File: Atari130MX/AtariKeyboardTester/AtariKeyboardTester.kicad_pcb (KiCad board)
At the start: 2 copper layers, 117 parts, among them J1 Conn_01x24, J2 Conn_02x12_Odd_Even, J3 Conn_01x26

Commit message: WIP keyboard tester
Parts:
- removed D12, D14, D15, D21, D23, D24, D28, D36, D43, D5, D50, D56, D57, D61, D64, D8, D_COL_1, D_COL_10, D_COL_11, D_COL_12, D_COL_13, D_COL_2, D_COL_3, D_COL_4, D_COL_5, D_COL_6, D_COL_7, D_COL_8, D_COL_9, D_ROW_1, D_ROW_10, D_ROW_2, D_ROW_3, D_ROW_4, D_ROW_5, D_ROW_6, D_ROW_7, D_ROW_8, D_ROW_9: LED, LED_THT:LED_D3.0mm
- added D_1_1: LED, LED_THT:LED_D3.0mm, F.Cu at (25.4, 22.9)
- added D_2_1: LED, LED_THT:LED_D3.0mm, F.Cu at (30.5, 22.9)
- added D_3_1: LED, LED_THT:LED_D3.0mm, F.Cu at (35.6, 22.9)
- added D_=_1: LED, LED_THT:LED_D3.0mm, F.Cu at (83.8, 27.9)
- added D_A_10: LED, LED_THT:LED_D3.0mm, F.Cu at (163.4, 93.0)
- added D_A_11: LED, LED_THT:LED_D3.0mm, F.Cu at (132.3, 122.4)
- added D_A_12: LED, LED_THT:LED_D3.0mm, F.Cu at (157.5, 98.5)
- added D_A_13: LED, LED_THT:LED_D3.0mm, F.Cu at (125.2, 129.2)
- added D_A_14: LED, LED_THT:LED_D3.0mm, F.Cu at (151.0, 104.1)
- added D_A_15: LED, LED_THT:LED_D3.0mm, F.Cu at (101.6, 152.5)
- added D_A_16: LED, LED_THT:LED_D3.0mm, F.Cu at (128.6, 116.9)
- added D_A_17: LED, LED_THT:LED_D3.0mm, F.Cu at (135.2, 110.8)
- added D_A_18: LED, LED_THT:LED_D3.0mm, F.Cu at (141.1, 110.2)
- added D_A_19: LED, LED_THT:LED_D3.0mm, F.Cu at (134.5, 116.9)
- added D_A_2: LED, LED_THT:LED_D3.0mm, F.Cu at (116.8, 118.1)
- added D_A_20: LED, LED_THT:LED_D3.0mm, F.Cu at (101.6, 147.0)
- added D_A_21: LED, LED_THT:LED_D3.0mm, F.Cu at (95.7, 155.7)
- added D_A_22: LED, LED_THT:LED_D3.0mm, F.Cu at (112.8, 141.4)
- added D_A_23: LED, LED_THT:LED_D3.0mm, F.Cu at (157.5, 93.0)
- added D_A_24: LED, LED_THT:LED_D3.0mm, F.Cu at (126.4, 123.7)
- added D_A_25: LED, LED_THT:LED_D3.0mm, F.Cu at (151.6, 98.5)
- added D_A_3: LED, LED_THT:LED_D3.0mm, F.Cu at (118.7, 135.9)
- added D_A_4: LED, LED_THT:LED_D3.0mm, F.Cu at (132.3, 128.0)
- added D_A_5: LED, LED_THT:LED_D3.0mm, F.Cu at (107.5, 152.5)
- added D_A_6: LED, LED_THT:LED_D3.0mm, F.Cu at (125.2, 134.8)
- added D_A_7: LED, LED_THT:LED_D3.0mm, F.Cu at (118.7, 141.4)
- added D_A_8: LED, LED_THT:LED_D3.0mm, F.Cu at (141.1, 115.8)
- added D_A_9: LED, LED_THT:LED_D3.0mm, F.Cu at (146.9, 109.7)
- added D_B_10: LED, LED_THT:LED_D3.0mm, F.Cu at (151.6, 93.0)
- added D_B_11: LED, LED_THT:LED_D3.0mm, F.Cu at (120.5, 123.7)
- added D_B_12: LED, LED_THT:LED_D3.0mm, F.Cu at (106.9, 135.9)
- added D_B_13: LED, LED_THT:LED_D3.0mm, F.Cu at (129.2, 111.3)
- added D_B_14: LED, LED_THT:LED_D3.0mm, F.Cu at (139.2, 104.7)
- added D_B_15: LED, LED_THT:LED_D3.0mm, F.Cu at (145.7, 98.5)
- added D_B_16: LED, LED_THT:LED_D3.0mm, F.Cu at (89.8, 150.1)
- added D_B_17: LED, LED_THT:LED_D3.0mm, F.Cu at (95.7, 144.6)
- added D_B_18: LED, LED_THT:LED_D3.0mm, F.Cu at (122.7, 118.1)
- added D_B_19: LED, LED_THT:LED_D3.0mm, F.Cu at (113.4, 130.3)
- added D_B_2: LED, LED_THT:LED_D3.0mm, F.Cu at (145.1, 104.1)
- added D_B_20: LED, LED_THT:LED_D3.0mm, F.Cu at (101.0, 132.4)
- added D_B_21: LED, LED_THT:LED_D3.0mm, F.Cu at (89.8, 144.6)
- added D_B_22: LED, LED_THT:LED_D3.0mm, F.Cu at (145.7, 93.0)
- added D_B_23: LED, LED_THT:LED_D3.0mm, F.Cu at (139.2, 99.1)
- added D_B_24: LED, LED_THT:LED_D3.0mm, F.Cu at (123.3, 111.3)
- added D_B_25: LED, LED_THT:LED_D3.0mm, F.Cu at (132.7, 105.2)
- added D_B_3: LED, LED_THT:LED_D3.0mm, F.Cu at (119.3, 130.3)
- added D_B_4: LED, LED_THT:LED_D3.0mm, F.Cu at (89.8, 155.7)
- added D_B_5: LED, LED_THT:LED_D3.0mm, F.Cu at (95.7, 150.1)
- added D_B_6: LED, LED_THT:LED_D3.0mm, F.Cu at (107.5, 147.0)
- added D_B_7: LED, LED_THT:LED_D3.0mm, F.Cu at (107.5, 130.3)
- added D_B_8: LED, LED_THT:LED_D3.0mm, F.Cu at (106.9, 141.4)
- added D_B_9: LED, LED_THT:LED_D3.0mm, F.Cu at (112.8, 135.9)
- added D_E_1: LED, LED_THT:LED_D3.0mm, F.Cu at (38.1, 27.9)
- added D_Fn_1: LED, LED_THT:LED_D3.0mm, F.Cu at (53.3, 15.2)
- added D_Fn_2: LED, LED_THT:LED_D3.0mm, F.Cu at (58.4, 15.2)
- added D_Fn_3: LED, LED_THT:LED_D3.0mm, F.Cu at (63.5, 15.2)
- added D_Fn_4: LED, LED_THT:LED_D3.0mm, F.Cu at (68.6, 15.2)
- added D_Help_1: LED, LED_THT:LED_D3.0mm, F.Cu at (76.2, 15.2)
- added D_Option_1: LED, LED_THT:LED_D3.0mm, F.Cu at (91.4, 15.2)
- added D_Reset_1: LED, LED_THT:LED_D3.0mm, F.Cu at (101.0, 137.9)
- added D_Return_1: LED, LED_THT:LED_D3.0mm, F.Cu at (90.2, 27.9)
- added D_Select_1: LED, LED_THT:LED_D3.0mm, F.Cu at (86.4, 15.2)
- added D_Start_1: LED, LED_THT:LED_D3.0mm, F.Cu at (81.3, 15.2)
- added D_T_1: LED, LED_THT:LED_D3.0mm, F.Cu at (48.3, 27.9)
- added D_V_1: LED, LED_THT:LED_D3.0mm, F.Cu at (47.0, 38.1)
- added J2: Conn_01x24, Connector_PinHeader_2.54mm:PinHeader_1x24_P2.54mm_Vertical, F.Cu at (222.2, 36.8)
- added Q_COL_1: Q_PNP_EBC, Package_TO_SOT_THT:TO-92_HandSolder, F.Cu at (126.5, 93.8)
- added Q_COL_10: Q_PNP_EBC, Package_TO_SOT_THT:TO-92_HandSolder, F.Cu at (107.8, 125.0)
- added Q_COL_11: Q_PNP_EBC, Package_TO_SOT_THT:TO-92_HandSolder, F.Cu at (101.3, 127.0)
- added Q_COL_12: Q_PNP_EBC, Package_TO_SOT_THT:TO-92_HandSolder, F.Cu at (126.5, 106.0)
- added Q_COL_13: Q_PNP_EBC, Package_TO_SOT_THT:TO-92_HandSolder, F.Cu at (133.0, 99.9)
- added Q_COL_14: Q_PNP_EBC, Package_TO_SOT_THT:TO-92_HandSolder, F.Cu at (139.5, 93.8)
- added Q_COL_2: Q_PNP_EBC, Package_TO_SOT_THT:TO-92_HandSolder, F.Cu at (104.1, 118.9)
- added Q_COL_3: Q_PNP_EBC, Package_TO_SOT_THT:TO-92_HandSolder, F.Cu at (120.0, 93.8)
- added Q_COL_4: Q_PNP_EBC, Package_TO_SOT_THT:TO-92_HandSolder, F.Cu at (88.3, 133.2)
- added Q_COL_5: Q_PNP_EBC, Package_TO_SOT_THT:TO-92_HandSolder, F.Cu at (88.3, 127.0)
- added Q_COL_6: Q_PNP_EBC, Package_TO_SOT_THT:TO-92_HandSolder, F.Cu at (104.1, 112.8)
- added Q_COL_7: Q_PNP_EBC, Package_TO_SOT_THT:TO-92_HandSolder, F.Cu at (94.8, 127.0)
- added Q_COL_8: Q_PNP_EBC, Package_TO_SOT_THT:TO-92_HandSolder, F.Cu at (120.0, 106.0)
- added Q_COL_9: Q_PNP_EBC, Package_TO_SOT_THT:TO-92_HandSolder, F.Cu at (114.3, 125.0)
- added Q_ROW_1: Q_NPN_EBC, Package_TO_SOT_THT:TO-92_HandSolder, F.Cu at (94.8, 139.3)
- added Q_ROW_2: Q_NPN_EBC, Package_TO_SOT_THT:TO-92_HandSolder, F.Cu at (110.6, 118.9)
- added Q_ROW_3: Q_NPN_EBC, Package_TO_SOT_THT:TO-92_HandSolder, F.Cu at (94.8, 133.2)
- added Q_ROW_4: Q_NPN_EBC, Package_TO_SOT_THT:TO-92_HandSolder, F.Cu at (126.5, 99.9)
- added Q_ROW_5: Q_NPN_EBC, Package_TO_SOT_THT:TO-92_HandSolder, F.Cu at (133.0, 93.8)
- added Q_ROW_6: Q_NPN_EBC, Package_TO_SOT_THT:TO-92_HandSolder, F.Cu at (88.3, 139.3)
- added Q_ROW_7: Q_NPN_EBC, Package_TO_SOT_THT:TO-92_HandSolder, F.Cu at (120.0, 99.9)
- added Q_ROW_8: Q_NPN_EBC, Package_TO_SOT_THT:TO-92_HandSolder, F.Cu at (110.6, 112.8)
- added Q_ROW_9: Q_NPN_EBC, Package_TO_SOT_THT:TO-92_HandSolder, F.Cu at (83.6, 150.8)
- added R10: R, Resistor_THT:R_Axial_DIN0207_L6.3mm_D2.5mm_P7.62mm_Horizontal, F.Cu at (56.2, 121.1)
- added R11: R, Resistor_THT:R_Axial_DIN0207_L6.3mm_D2.5mm_P7.62mm_Horizontal, F.Cu at (72.0, 135.3)
- added R12: R, Resistor_THT:R_Axial_DIN0207_L6.3mm_D2.5mm_P7.62mm_Horizontal, F.Cu at (56.2, 125.8)
- added R13: R, Resistor_THT:R_Axial_DIN0207_L6.3mm_D2.5mm_P7.62mm_Horizontal, F.Cu at (87.9, 121.1)
- added R14: R, Resistor_THT:R_Axial_DIN0207_L6.3mm_D2.5mm_P7.62mm_Horizontal, F.Cu at (72.0, 121.1)
- added R15: R, Resistor_THT:R_Axial_DIN0207_L6.3mm_D2.5mm_P7.62mm_Horizontal, F.Cu at (87.9, 102.1)
- added R16: R, Resistor_THT:R_Axial_DIN0207_L6.3mm_D2.5mm_P7.62mm_Horizontal, F.Cu at (56.2, 144.8)
- added R17: R, Resistor_THT:R_Axial_DIN0207_L6.3mm_D2.5mm_P7.62mm_Horizontal, F.Cu at (56.2, 92.6)
- added R18: R, Resistor_THT:R_Axial_DIN0207_L6.3mm_D2.5mm_P7.62mm_Horizontal, F.Cu at (72.0, 92.6)
- added R19: R, Resistor_THT:R_Axial_DIN0207_L6.3mm_D2.5mm_P7.62mm_Horizontal, F.Cu at (87.9, 92.6)
- added R2: R, Resistor_THT:R_Axial_DIN0207_L6.3mm_D2.5mm_P7.62mm_Horizontal, F.Cu at (72.0, 140.1)
- added R20: R, Resistor_THT:R_Axial_DIN0207_L6.3mm_D2.5mm_P7.62mm_Horizontal, F.Cu at (72.0, 111.6)
- added R21: R, Resistor_THT:R_Axial_DIN0207_L6.3mm_D2.5mm_P7.62mm_Horizontal, F.Cu at (87.9, 116.3)
- added R22: R, Resistor_THT:R_Axial_DIN0207_L6.3mm_D2.5mm_P7.62mm_Horizontal, F.Cu at (72.0, 116.3)
- added R23: R, Resistor_THT:R_Axial_DIN0207_L6.3mm_D2.5mm_P7.62mm_Horizontal, F.Cu at (56.2, 116.3)
- added R24: R, Resistor_THT:R_Axial_DIN0207_L6.3mm_D2.5mm_P7.62mm_Horizontal, F.Cu at (87.9, 111.6)
- added R3: R, Resistor_THT:R_Axial_DIN0207_L6.3mm_D2.5mm_P7.62mm_Horizontal, F.Cu at (72.0, 144.8)
- added R4: R, Resistor_THT:R_Axial_DIN0207_L6.3mm_D2.5mm_P7.62mm_Horizontal, F.Cu at (56.2, 149.6)
- added R5: R, Resistor_THT:R_Axial_DIN0207_L6.3mm_D2.5mm_P7.62mm_Horizontal, F.Cu at (56.2, 140.1)
- added R6: R, Resistor_THT:R_Axial_DIN0207_L6.3mm_D2.5mm_P7.62mm_Horizontal, F.Cu at (56.2, 135.3)
- added R7: R, Resistor_THT:R_Axial_DIN0207_L6.3mm_D2.5mm_P7.62mm_Horizontal, F.Cu at (72.0, 130.6)
- added R8: R, Resistor_THT:R_Axial_DIN0207_L6.3mm_D2.5mm_P7.62mm_Horizontal, F.Cu at (56.2, 130.6)
- added R9: R, Resistor_THT:R_Axial_DIN0207_L6.3mm_D2.5mm_P7.62mm_Horizontal, F.Cu at (72.0, 125.8)
- added R_LED_COL_1: R, Resistor_THT:R_Axial_DIN0207_L6.3mm_D2.5mm_P7.62mm_Horizontal, F.Cu at (103.7, 92.6)
- added R_LED_COL_10: R, Resistor_THT:R_Axial_DIN0207_L6.3mm_D2.5mm_P7.62mm_Horizontal, F.Cu at (56.2, 102.1)
- added R_LED_COL_11: R, Resistor_THT:R_Axial_DIN0207_L6.3mm_D2.5mm_P7.62mm_Horizontal, F.Cu at (103.7, 97.3)
- added R_LED_COL_12: R, Resistor_THT:R_Axial_DIN0207_L6.3mm_D2.5mm_P7.62mm_Horizontal, F.Cu at (87.9, 97.3)
- added R_LED_COL_13: R, Resistor_THT:R_Axial_DIN0207_L6.3mm_D2.5mm_P7.62mm_Horizontal, F.Cu at (72.0, 97.3)
- added R_LED_COL_14: R, Resistor_THT:R_Axial_DIN0207_L6.3mm_D2.5mm_P7.62mm_Horizontal, F.Cu at (56.2, 97.3)
- added R_LED_COL_2: R, Resistor_THT:R_Axial_DIN0207_L6.3mm_D2.5mm_P7.62mm_Horizontal, F.Cu at (56.2, 111.6)
- added R_LED_COL_3: R, Resistor_THT:R_Axial_DIN0207_L6.3mm_D2.5mm_P7.62mm_Horizontal, F.Cu at (103.7, 106.8)
- added R_LED_COL_4: R, Resistor_THT:R_Axial_DIN0207_L6.3mm_D2.5mm_P7.62mm_Horizontal, F.Cu at (87.9, 106.8)
- added R_LED_COL_5: R, Resistor_THT:R_Axial_DIN0207_L6.3mm_D2.5mm_P7.62mm_Horizontal, F.Cu at (72.0, 106.8)
- added R_LED_COL_6: R, Resistor_THT:R_Axial_DIN0207_L6.3mm_D2.5mm_P7.62mm_Horizontal, F.Cu at (56.2, 106.8)
- added R_LED_COL_7: R, Resistor_THT:R_Axial_DIN0207_L6.3mm_D2.5mm_P7.62mm_Horizontal, F.Cu at (103.7, 102.1)
- added R_LED_COL_8: R, Resistor_THT:R_Axial_DIN0207_L6.3mm_D2.5mm_P7.62mm_Horizontal, F.Cu at (51.5, 155.7)
- added R_LED_COL_9: R, Resistor_THT:R_Axial_DIN0207_L6.3mm_D2.5mm_P7.62mm_Horizontal, F.Cu at (72.0, 102.1)
- R1: footprint Resistor_THT:R_Axial_DIN0204_L3.6mm_D1.6mm_P5.08mm_Horizontal -> Resistor_THT:R_Axial_DIN0207_L6.3mm_D2.5mm_P7.62mm_Horizontal
- moved JP24 189.2 mm to (280.7, 43.2), turned to 90 degrees
- moved JP18 184.1 mm to (265.4, 43.2), turned to 90 degrees
- moved R1 178.4 mm to (67.4, 154.3)
- moved JP22 177.6 mm to (275.6, 43.2), turned to 90 degrees
- moved JP16 172.8 mm to (260.4, 43.2), turned to 90 degrees
- moved JP20 166.0 mm to (270.5, 43.2), turned to 90 degrees
- moved JP23 154.9 mm to (278.1, 43.2), turned to 90 degrees
- moved JP9 145.5 mm to (242.6, 43.2), turned to 90 degrees
- moved JP21 144.1 mm to (273.1, 43.2), turned to 90 degrees
- moved JP11 143.8 mm to (247.7, 43.2), turned to 90 degrees
- moved JP2 143.6 mm to (224.8, 43.2), turned to 90 degrees
- moved JP14 138.0 mm to (255.3, 43.2), turned to 90 degrees
- moved JP19 133.6 mm to (268.0, 43.2), turned to 90 degrees
- moved JP17 124.3 mm to (262.9, 43.2), turned to 90 degrees
- moved JP6 124.2 mm to (234.9, 43.2), turned to 90 degrees
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- renumbered D59 to D_*_1, D54 to D_+_1, D42 to D_,_1, D53 to D_-_1, D47 to D_._1, D52 to D_/_1, D46 to D_0_1, D17 to D_4_1, D22 to D_5_1, D26 to D_6_1, D31 to D_7_1, D37 to D_8_1, D41 to D_9_1, D49 to D_;_1, D51 to D_<_1, D55 to D_>_1, D7 to D_A_1, D27 to D_B_1, D65 to D_Break_1, D18 to D_C_1, D62 to D_Caps_1, D3 to D_Control_1, D16 to D_D_1, D60 to D_Del_1, D1 to D_Esc_1, D20 to D_F_1, D25 to D_G_1, D30 to D_H_1, D39 to D_I_1, D63 to D_Inv_1, D35 to D_J_1, D40 to D_K_1, D_COL_14 to D_LED_1, D45 to D_L_1, D38 to D_M_1, D33 to D_N_1, D44 to D_O_1, D48 to D_P_1, D6 to D_Q_1, D19 to D_R_1, D32 to D_SPACE_1, D11 to D_S_1, D4 to D_Shift_1, D58 to D_Shift_2, D2 to D_Tab_1, D34 to D_U_1, D10 to D_W_1, D13 to D_X_1, D29 to D_Y_1, D9 to D_Z_1, J2 to J3, J3 to J4
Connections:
- D_*_1 pad 1: Net-(D59-Pad1) -> LED_ROW_5
- D_*_1 pad 2: Net-(D59-Pad2) -> LED_COL_7
- D_+_1 pad 1: Net-(D54-Pad1) -> LED_ROW_5
- D_+_1 pad 2: Net-(D54-Pad2) -> LED_COL_6
- D_,_1 pad 1: Net-(D42-Pad1) -> LED_ROW_7
- D_,_1 pad 2: Net-(D42-Pad2) -> LED_COL_4
- D_-_1 pad 1: Net-(D53-Pad1) -> LED_ROW_3
- D_-_1 pad 2: Net-(D53-Pad2) -> LED_COL_6
- D_._1 pad 1: Net-(D47-Pad1) -> LED_ROW_7
- D_._1 pad 2: Net-(D47-Pad2) -> LED_COL_5
- D_/_1 pad 1: Net-(D52-Pad1) -> LED_ROW_7
- D_/_1 pad 2: Net-(D52-Pad2) -> LED_COL_6
- D_0_1 pad 1: Net-(D46-Pad1) -> LED_ROW_1
- D_0_1 pad 2: Net-(D46-Pad2) -> LED_COL_5
- D_4_1 pad 1: Net-(D17-Pad1) -> LED_ROW_2
- D_4_1 pad 2: Net-(D17-Pad2) -> LED_COL_4
- D_5_1 pad 1: Net-(D22-Pad1) -> LED_ROW_2
- D_5_1 pad 2: Net-(D22-Pad2) -> LED_COL_3
- D_6_1 pad 1: Net-(D26-Pad1) -> LED_ROW_2
- D_6_1 pad 2: Net-(D26-Pad2) -> LED_COL_1
- D_7_1 pad 1: Net-(D31-Pad1) -> LED_ROW_1
- D_7_1 pad 2: Net-(D31-Pad2) -> LED_COL_1
- D_8_1 pad 1: Net-(D37-Pad1) -> LED_ROW_1
- D_8_1 pad 2: Net-(D37-Pad2) -> LED_COL_3
- D_9_1 pad 1: Net-(D41-Pad1) -> LED_ROW_1
- D_9_1 pad 2: Net-(D41-Pad2) -> LED_COL_4
- D_;_1 pad 1: Net-(D49-Pad1) -> LED_ROW_5
- D_;_1 pad 2: Net-(D49-Pad2) -> LED_COL_5
- D_<_1 pad 1: Net-(D51-Pad1) -> LED_ROW_1
- D_<_1 pad 2: Net-(D51-Pad2) -> LED_COL_6
- D_>_1 pad 1: Net-(D55-Pad1) -> LED_ROW_1
- D_>_1 pad 2: Net-(D55-Pad2) -> LED_COL_7
- D_A_1 pad 1: Net-(D7-Pad1) -> LED_ROW_6
- D_A_1 pad 2: Net-(D7-Pad2) -> LED_COL_7
- D_B_1 pad 1: Net-(D27-Pad1) -> LED_ROW_8
- D_B_1 pad 2: Net-(D27-Pad2) -> LED_COL_3
- D_Break_1 pad 1: Net-(D65-Pad1) -> LED_ROW_1
- D_Break_1 pad 2: Net-(D65-Pad2) -> LED_COL_9
- D_C_1 pad 1: Net-(D18-Pad1) -> LED_ROW_8
- D_C_1 pad 2: Net-(D18-Pad2) -> LED_COL_5
- D_Caps_1 pad 1: Net-(D62-Pad1) -> LED_ROW_6
- D_Caps_1 pad 2: Net-(D62-Pad2) -> LED_COL_8
- D_Control_1 pad 1: Net-(D3-Pad1) -> LED_ROW_5
- D_Control_1 pad 2: Net-(D3-Pad2) -> LED_COL_9
- D_D_1 pad 1: Net-(D16-Pad1) -> LED_ROW_6
- D_D_1 pad 2: Net-(D16-Pad2) -> LED_COL_5
- D_Del_1 pad 1: Net-(D60-Pad1) -> LED_ROW_1
- D_Del_1 pad 2: Net-(D60-Pad2) -> LED_COL_8
- D_Esc_1 pad 1: Net-(D1-Pad1) -> LED_ROW_2
- D_Esc_1 pad 2: Net-(D1-Pad2) -> LED_COL_8
- D_F_1 pad 1: Net-(D20-Pad1) -> LED_ROW_6
- D_F_1 pad 2: Net-(D20-Pad2) -> LED_COL_4
- D_G_1 pad 1: Net-(D25-Pad1) -> LED_ROW_6
- D_G_1 pad 2: Net-(D25-Pad2) -> LED_COL_3
- D_H_1 pad 1: Net-(D30-Pad1) -> LED_ROW_6
- D_H_1 pad 2: Net-(D30-Pad2) -> LED_COL_2
- D_I_1 pad 1: Net-(D39-Pad1) -> LED_ROW_3
- D_I_1 pad 2: Net-(D39-Pad2) -> LED_COL_3
- D_Inv_1 pad 1: Net-(D63-Pad1) -> LED_ROW_7
- D_Inv_1 pad 2: Net-(D63-Pad2) -> LED_COL_7
- D_J_1 pad 1: Net-(D35-Pad1) -> LED_ROW_5
- D_J_1 pad 2: Net-(D35-Pad2) -> LED_COL_2
- D_K_1 pad 1: Net-(D40-Pad1) -> LED_ROW_5
- D_K_1 pad 2: Net-(D40-Pad2) -> LED_COL_3
- D_LED_1 pad 1: Net-(D_COL_14-Pad1) -> GND
- D_LED_1 pad 2: Net-(D_COL_14-Pad2) -> LED_COL_14
- D_L_1 pad 1: Net-(D45-Pad1) -> LED_ROW_5
- D_L_1 pad 2: Net-(D45-Pad2) -> LED_COL_4
- D_M_1 pad 1: Net-(D38-Pad1) -> LED_ROW_7
- D_M_1 pad 2: Net-(D38-Pad2) -> LED_COL_3
- D_N_1 pad 1: Net-(D33-Pad1) -> LED_ROW_7
- D_N_1 pad 2: Net-(D33-Pad2) -> LED_COL_1
- D_O_1 pad 1: Net-(D44-Pad1) -> LED_ROW_3
- D_O_1 pad 2: Net-(D44-Pad2) -> LED_COL_4
- D_P_1 pad 1: Net-(D48-Pad1) -> LED_ROW_3
- D_P_1 pad 2: Net-(D48-Pad2) -> LED_COL_5
- D_Q_1 pad 1: Net-(D6-Pad1) -> LED_ROW_4
- D_Q_1 pad 2: Net-(D6-Pad2) -> LED_COL_7
- D_R_1 pad 1: Net-(D19-Pad1) -> LED_ROW_4
- D_R_1 pad 2: Net-(D19-Pad2) -> LED_COL_4
- D_SPACE_1 pad 1: Net-(D32-Pad1) -> LED_ROW_7
- D_SPACE_1 pad 2: Net-(D32-Pad2) -> LED_COL_2
- D_S_1 pad 1: Net-(D11-Pad1) -> LED_ROW_6
- D_S_1 pad 2: Net-(D11-Pad2) -> LED_COL_6
- D_Shift_1 pad 1: Net-(D4-Pad1) -> LED_ROW_8
- D_Shift_1 pad 2: Net-(D4-Pad2) -> LED_COL_9
- D_Shift_2 pad 1: Net-(D58-Pad1) -> LED_ROW_8
- D_Shift_2 pad 2: Net-(D58-Pad2) -> LED_COL_9
- D_Tab_1 pad 1: Net-(D2-Pad1) -> LED_ROW_4
- D_Tab_1 pad 2: Net-(D2-Pad2) -> LED_COL_8
- D_U_1 pad 1: Net-(D34-Pad1) -> LED_ROW_3
- D_U_1 pad 2: Net-(D34-Pad2) -> LED_COL_1
- D_W_1 pad 1: Net-(D10-Pad1) -> LED_ROW_4
- D_W_1 pad 2: Net-(D10-Pad2) -> LED_COL_6
- D_X_1 pad 1: Net-(D13-Pad1) -> LED_ROW_8
- D_X_1 pad 2: Net-(D13-Pad2) -> LED_COL_6
- D_Y_1 pad 1: Net-(D29-Pad1) -> LED_ROW_4
- D_Y_1 pad 2: Net-(D29-Pad2) -> LED_COL_1
- D_Z_1 pad 1: Net-(D9-Pad1) -> LED_ROW_8
- D_Z_1 pad 2: Net-(D9-Pad2) -> LED_COL_7
- J1 pad 1: Net-(J1-Pad1) -> CONN_1
- J1 pad 10: Net-(J1-Pad10) -> CONN_10
- J1 pad 11: Net-(J1-Pad11) -> CONN_11
- J1 pad 12: Net-(J1-Pad12) -> CONN_12
- J1 pad 13: Net-(J1-Pad13) -> CONN_13
- J1 pad 14: Net-(J1-Pad14) -> CONN_14
- J1 pad 15: Net-(J1-Pad15) -> CONN_15
- J1 pad 16: Net-(J1-Pad16) -> CONN_16
- J1 pad 17: Net-(J1-Pad17) -> CONN_17
- J1 pad 18: Net-(J1-Pad18) -> CONN_18
- J1 pad 19: Net-(J1-Pad19) -> CONN_19
- J1 pad 2: Net-(J1-Pad2) -> CONN_2
- J1 pad 20: Net-(J1-Pad20) -> CONN_20
- J1 pad 21: Net-(J1-Pad21) -> CONN_21
- J1 pad 22: Net-(J1-Pad22) -> CONN_22
- J1 pad 23: Net-(J1-Pad23) -> CONN_23
- J1 pad 24: Net-(J1-Pad24) -> CONN_24
- J1 pad 3: Net-(J1-Pad3) -> CONN_3
- J1 pad 4: Net-(J1-Pad4) -> CONN_4
- J1 pad 5: Net-(J1-Pad5) -> CONN_5
- J1 pad 6: Net-(J1-Pad6) -> CONN_6
- J1 pad 7: Net-(J1-Pad7) -> CONN_7
- J1 pad 8: Net-(J1-Pad8) -> CONN_8
- J1 pad 9: Net-(J1-Pad9) -> CONN_9
- J3 pad 1: Net-(J2-Pad1) -> CONN_1
- J3 pad 10: Net-(J2-Pad10) -> CONN_10
- J3 pad 11: Net-(J2-Pad11) -> CONN_11
- J3 pad 12: Net-(J2-Pad12) -> CONN_12
- J3 pad 13: Net-(J2-Pad13) -> CONN_13
- J3 pad 14: Net-(J2-Pad14) -> CONN_14
- J3 pad 15: Net-(J2-Pad15) -> CONN_15
- J3 pad 16: Net-(J2-Pad16) -> CONN_16
- J3 pad 17: Net-(J2-Pad17) -> CONN_17
- J3 pad 18: Net-(J2-Pad18) -> CONN_18
- J3 pad 19: Net-(J2-Pad19) -> CONN_19
- J3 pad 2: Net-(J2-Pad2) -> CONN_2
- J3 pad 20: Net-(J2-Pad20) -> CONN_20
- J3 pad 21: Net-(J2-Pad21) -> CONN_21
- J3 pad 22: Net-(J2-Pad22) -> CONN_22
- J3 pad 23: Net-(J2-Pad23) -> CONN_23
- J3 pad 24: Net-(J2-Pad24) -> CONN_24
- J3 pad 3: Net-(J2-Pad3) -> CONN_3
- J3 pad 4: Net-(J2-Pad4) -> CONN_4
- J3 pad 5: Net-(J2-Pad5) -> CONN_5
- J3 pad 6: Net-(J2-Pad6) -> CONN_6
- J3 pad 7: Net-(J2-Pad7) -> CONN_7
- J3 pad 8: Net-(J2-Pad8) -> CONN_8
- J3 pad 9: Net-(J2-Pad9) -> CONN_9
- J4 pad 1: Net-(J3-Pad1) -> CONN_1
- J4 pad 10: Net-(J3-Pad10) -> CONN_10
- J4 pad 11: Net-(J3-Pad11) -> CONN_11
- J4 pad 12: Net-(J3-Pad12) -> CONN_12
- J4 pad 13: Net-(J3-Pad13) -> CONN_13
- J4 pad 14: Net-(J3-Pad14) -> CONN_14
- J4 pad 15: Net-(J3-Pad15) -> CONN_15
- J4 pad 16: Net-(J3-Pad16) -> CONN_16
- J4 pad 17: Net-(J3-Pad17) -> CONN_17
- J4 pad 18: Net-(J3-Pad18) -> CONN_18
- J4 pad 19: Net-(J3-Pad19) -> CONN_19
- J4 pad 2: Net-(J3-Pad2) -> CONN_2
- J4 pad 20: Net-(J3-Pad20) -> CONN_20
- J4 pad 21: Net-(J3-Pad21) -> CONN_21
- J4 pad 22: Net-(J3-Pad22) -> CONN_22
- J4 pad 23: Net-(J3-Pad23) -> CONN_23
- J4 pad 24: Net-(J3-Pad24) -> CONN_24
- J4 pad 25: Net-(J3-Pad1) -> CONN_1
- J4 pad 26: Net-(J3-Pad26) -> CONN_3
- J4 pad 3: Net-(J3-Pad26) -> CONN_3
- J4 pad 4: Net-(J3-Pad4) -> CONN_4
- J4 pad 5: Net-(J3-Pad5) -> CONN_5
- J4 pad 6: Net-(J3-Pad6) -> CONN_6
- J4 pad 7: Net-(J3-Pad7) -> CONN_7
- J4 pad 8: Net-(J3-Pad8) -> CONN_8
- J4 pad 9: Net-(J3-Pad9) -> CONN_9
- JP1 pad 1: Net-(JP1-Pad1) -> ROW_1
- JP1 pad 2: Net-(JP1-Pad2) -> B_CONN_1
- JP10 pad 1: Net-(JP10-Pad1) -> COL_1
- JP10 pad 2: Net-(JP1-Pad2) -> B_CONN_10
- JP10 pad 3: Net-(JP10-Pad3) -> COL_5
- JP11 pad 1: Net-(JP11-Pad1) -> COL_2
- JP11 pad 2: GND -> B_CONN_11
- JP11 pad 3: Net-(JP11-Pad3) -> COL_6
- JP12 pad 1: Net-(JP12-Pad1) -> COL_3
- JP12 pad 2: GND -> B_CONN_12
- JP12 pad 3: Net-(JP12-Pad3) -> ROW_3
- JP13 pad 1: Net-(JP13-Pad1) -> COL_4
- JP13 pad 2: GND -> B_CONN_13
- JP13 pad 3: Net-(JP13-Pad3) -> ROW_1
- JP14 pad 1: Net-(JP14-Pad1) -> COL_5
- JP14 pad 2: GND -> B_CONN_14
- JP14 pad 3: Net-(JP14-Pad3) -> ROW_2
- JP15 pad 1: Net-(JP15-Pad1) -> COL_6
- JP15 pad 2: GND -> B_CONN_15
- JP15 pad 3: Net-(JP15-Pad3) -> ROW_4
- JP16 pad 1: Net-(JP16-Pad1) -> COL_7
- JP16 pad 2: GND -> B_CONN_16
- JP16 pad 3: Net-(JP16-Pad3) -> COL_8
- JP17 pad 1: Net-(JP17-Pad1) -> COL_8
- JP17 pad 2: GND -> B_CONN_17
- JP17 pad 3: Net-(JP17-Pad3) -> COL_7
- JP18 pad 1: Net-(JP18-Pad1) -> ROW_9
- JP18 pad 2: GND -> B_CONN_18
- JP18 pad 3: Net-(JP18-Pad3) -> ROW_6
- JP19 pad 2: GND -> B_CONN_19
- JP19 pad 3: Net-(JP19-Pad3) -> COL_1
- JP2 pad 1: Net-(JP2-Pad1) -> ROW_2
- JP2 pad 2: Net-(JP1-Pad2) -> B_CONN_2
- JP2 pad 3: Net-(JP2-Pad3) -> COL_14
- JP20 pad 1: Net-(JP20-Pad1) -> COL_10
- JP20 pad 2: GND -> B_CONN_20
- JP20 pad 3: Net-(JP20-Pad3) -> COL_9
- JP21 pad 1: Net-(JP21-Pad1) -> COL_11
- JP21 pad 2: GND -> B_CONN_21
- JP21 pad 3: Net-(JP21-Pad3) -> COL_10
- JP22 pad 1: Net-(JP22-Pad1) -> COL_12
- JP22 pad 2: GND -> B_CONN_22
- JP22 pad 3: Net-(JP22-Pad3) -> COL_11
- JP23 pad 1: Net-(JP23-Pad1) -> COL_13
- JP23 pad 2: GND -> B_CONN_23
- JP23 pad 3: Net-(JP23-Pad3) -> COL_12
- JP24 pad 1: Net-(JP24-Pad1) -> COL_14
- JP24 pad 2: GND -> B_CONN_24
- JP24 pad 3: Net-(JP24-Pad3) -> COL_13
- JP3 pad 1: Net-(JP3-Pad1) -> ROW_3
- JP3 pad 2: Net-(JP1-Pad2) -> B_CONN_3
- JP3 pad 3: Net-(JP3-Pad3) -> ROW_9
- JP4 pad 1: Net-(JP4-Pad1) -> ROW_4
- JP4 pad 2: Net-(JP1-Pad2) -> B_CONN_4
- JP4 pad 3: Net-(JP4-Pad3) -> COL_2
- JP5 pad 1: Net-(JP5-Pad1) -> ROW_5
- JP5 pad 2: Net-(JP1-Pad2) -> B_CONN_5
- JP5 pad 3: Net-(JP5-Pad3) -> ROW_7
- JP6 pad 1: Net-(JP6-Pad1) -> ROW_6
- JP6 pad 2: Net-(JP1-Pad2) -> B_CONN_6
- JP6 pad 3: Net-(JP6-Pad3) -> ROW_8
- JP7 pad 1: Net-(JP7-Pad1) -> ROW_7
- JP7 pad 2: Net-(JP1-Pad2) -> B_CONN_7
- JP7 pad 3: Net-(JP7-Pad3) -> ROW_5
- JP8 pad 1: Net-(JP8-Pad1) -> ROW_8
- JP8 pad 2: Net-(JP1-Pad2) -> B_CONN_8
- JP8 pad 3: Net-(JP8-Pad3) -> COL_3
- JP9 pad 1: Net-(JP9-Pad1) -> COL_9
- JP9 pad 2: Net-(JP1-Pad2) -> B_CONN_9
- JP9 pad 3: Net-(JP9-Pad3) -> COL_4
- R1 pad 1: Net-(JP1-Pad2) -> Net-(D_A_2-Pad1)
- R1 pad 2: +3V3 -> CONN_1

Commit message: WIP: routing the keyboard tester
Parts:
- moved J1 192.8 mm to (33.0, 67.3)
- moved JP10 192.5 mm to (55.9, 78.7)
- moved JP11 192.5 mm to (58.4, 78.7)
- moved JP14 192.5 mm to (66.0, 78.7)
- moved JP15 192.5 mm to (68.6, 78.7)
- moved JP16 192.5 mm to (71.1, 78.7)
- moved JP18 192.5 mm to (76.2, 78.7)
- moved JP19 192.5 mm to (78.7, 78.7)
- moved JP21 192.5 mm to (83.8, 78.7)
- moved JP24 192.5 mm to (91.4, 78.7)
- moved JP3 192.5 mm to (38.1, 78.7)
- moved JP4 192.5 mm to (40.6, 78.7)
- moved JP7 192.5 mm to (48.3, 78.8)
- moved JP8 192.5 mm to (50.8, 78.7)
- moved J2 192.5 mm to (33.0, 72.4)
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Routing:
- net CONN_22: track 0.00 -> 296.4 mm
- net CONN_23: track 0.00 -> 295.3 mm
- net CONN_20: track 0.00 -> 291.8 mm
- net CONN_21: track 0.00 -> 290.9 mm
- net CONN_3: track 0.00 -> 290.8 mm
- net CONN_18: track 0.00 -> 287.3 mm
- net CONN_19: track 0.00 -> 286.2 mm
- net CONN_16: track 0.00 -> 282.8 mm
- net CONN_17: track 0.00 -> 281.7 mm
- net CONN_14: track 0.00 -> 278.6 mm
- net CONN_15: track 0.00 -> 277.1 mm
- net CONN_12: track 0.00 -> 277.1 mm
- net CONN_13: track 0.00 -> 274.5 mm
- net CONN_2: track 0.00 -> 274.3 mm
- net CONN_1: track 0.00 -> 273.6 mm
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
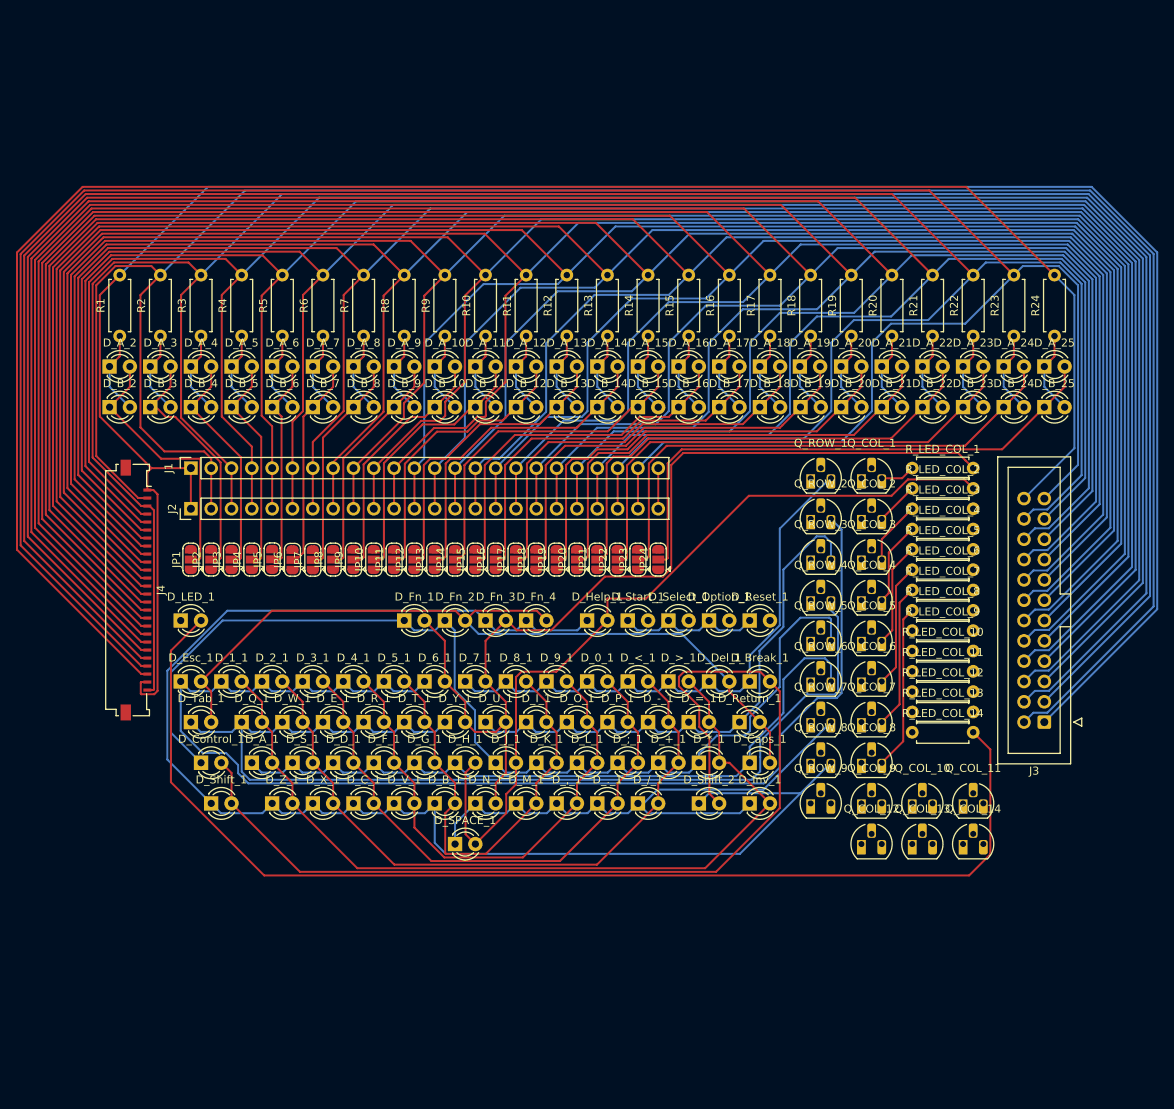
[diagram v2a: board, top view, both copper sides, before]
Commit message: More routing, replace solder headers with pin headers.
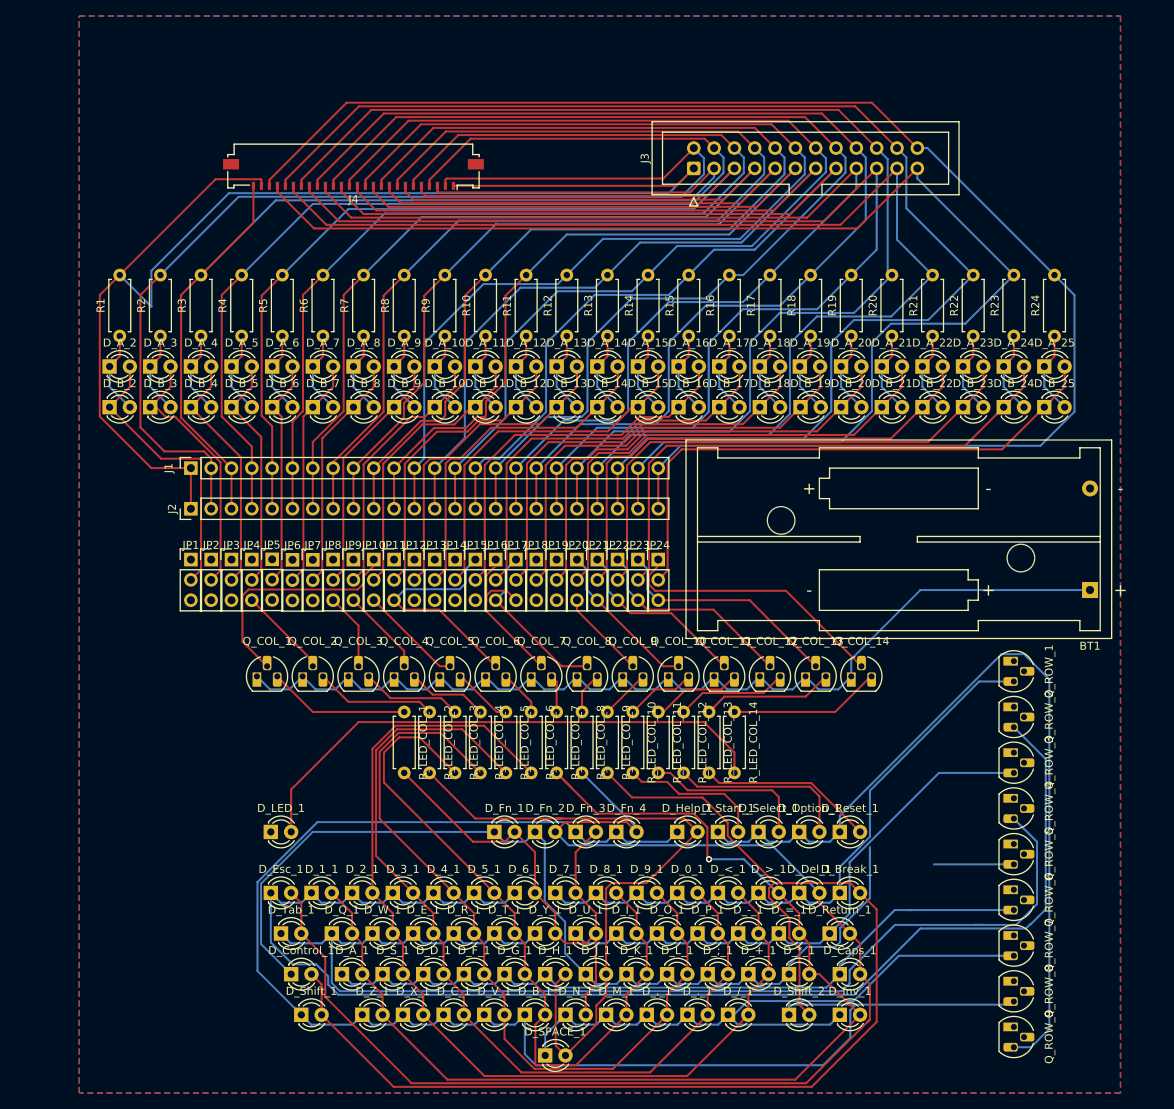
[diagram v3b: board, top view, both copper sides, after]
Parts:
- added BT1: Battery, Battery:BatteryHolder_Keystone_2468_2xAAA, F.Cu at (145.4, 82.5)
- JP1, JP10, JP11, JP12, JP13, JP14, JP15, JP16, JP17, JP18, JP19, JP2, JP20, JP21, JP22, JP23, JP24, JP3, JP4, JP5, JP6, JP7, JP8, JP9: footprint Jumper:SolderJumper-3_P1.3mm_Open_RoundedPad1.0x1.5mm -> AtariKeyboardTester:PinHeader_1x03_P2.54mm_Vertical
- moved J3 81.9 mm to (95.9, 29.8), turned to 90 degrees
- moved Q_COL_1 79.5 mm to (41.3, 93.3)
- moved Q_COL_2 72.6 mm to (47.0, 93.3)
- moved R_LED_COL_1 70.4 mm to (59.7, 97.8), turned to 270 degrees
- moved R_LED_COL_2 66.5 mm to (62.9, 97.8), turned to 270 degrees
- moved Q_COL_3 65.8 mm to (52.7, 93.3)
- moved R_LED_COL_3 62.5 mm to (66.0, 97.8), turned to 270 degrees
- moved Q_COL_4 59.2 mm to (58.4, 93.3)
- moved R_LED_COL_4 58.6 mm to (69.2, 97.8), turned to 270 degrees
- moved J4 57.9 mm to (53.3, 31.1), turned to 180 degrees
- moved R_LED_COL_5 54.7 mm to (72.4, 97.8), turned to 270 degrees
- moved Q_COL_5 52.9 mm to (64.1, 93.3)
- moved R_LED_COL_6 50.8 mm to (75.6, 97.8), turned to 270 degrees
- moved Q_COL_6 47.0 mm to (69.8, 93.3)
- moved R_LED_COL_7 47.0 mm to (78.7, 97.8), turned to 270 degrees
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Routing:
- net CONN_16: track 282.8 -> 141.1 mm
- net CONN_17: track 281.7 -> 140.6 mm
- net CONN_15: track 277.1 -> 136.8 mm
- net CONN_18: track 287.3 -> 146.9 mm
- net CONN_14: track 278.6 -> 139.3 mm
- net CONN_19: track 286.2 -> 147.5 mm
- net CONN_13: track 274.5 -> 136.3 mm
- net CONN_20: track 291.8 -> 154.4 mm
- net CONN_12: track 277.1 -> 139.9 mm
- net CONN_3: track 290.8 -> 153.6 mm
- net CONN_11: track 270.4 -> 134.4 mm
- net CONN_10: track 271.5 -> 136.4 mm
- net CONN_9: track 265.9 -> 132.1 mm
- net CONN_8: track 268.5 -> 135.6 mm
- net CONN_21: track 290.9 -> 158.1 mm
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- added copper zone on B.Cu, net GND
- added copper zone on F.Cu, net GND

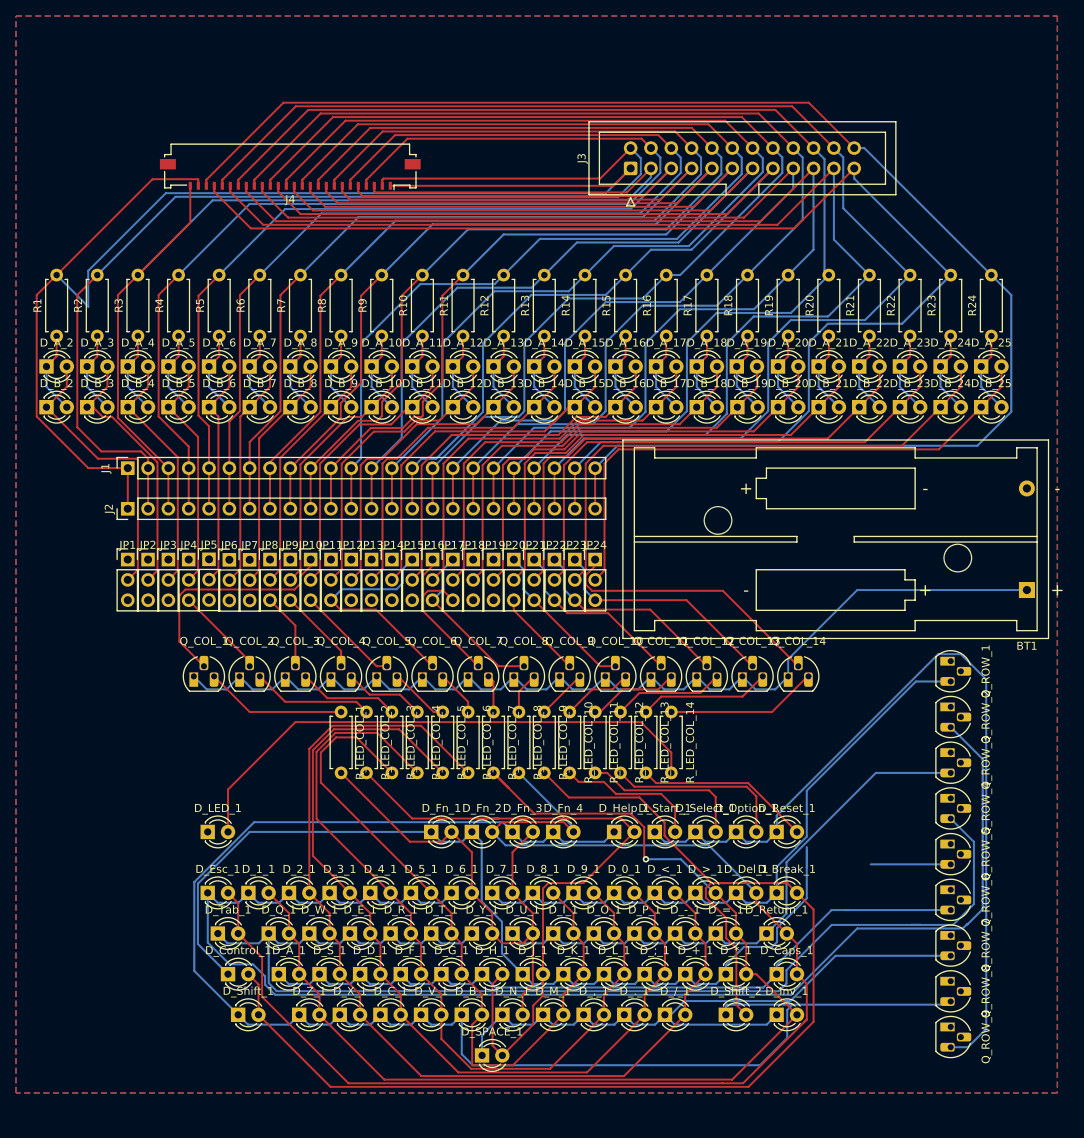
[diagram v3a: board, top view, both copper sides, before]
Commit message: Keyboard test rig routing finished, some silkscreen work
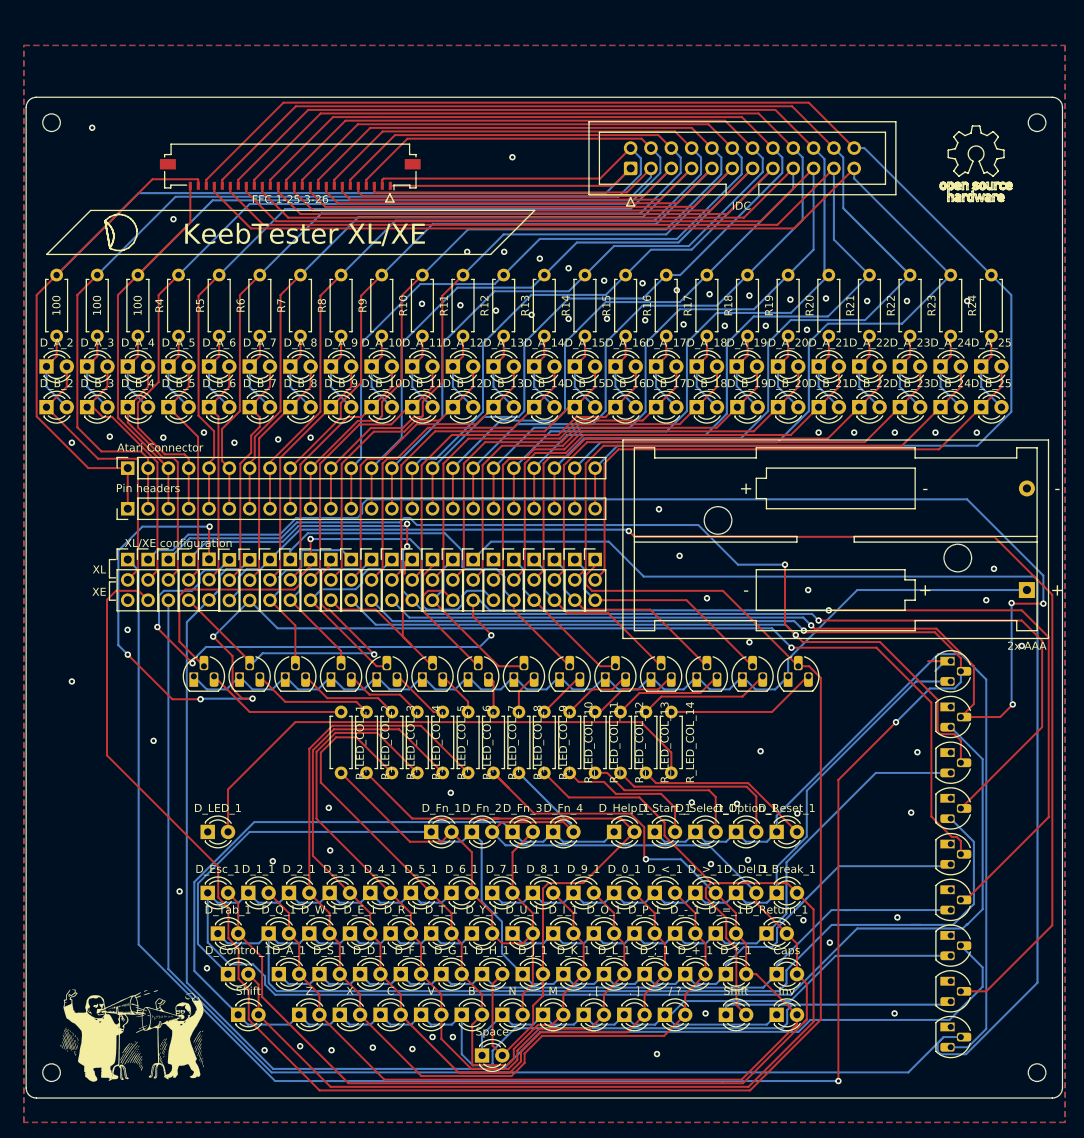
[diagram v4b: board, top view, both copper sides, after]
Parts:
- removed JP1: SolderJumper_3_Open, AtariKeyboardTester:PinHeader_1x03_P2.54mm_Vertical
- added G***: LOGO, Atari130MX:ScreamingAtTheRadio, F.Cu at (33.7, 137.2)
- added Matrix: Atari_XL_XE_Matrix, AtariKeyboardTester:Atari_XL_XE_Matrix, B.Cu at (57.1, 33.0)
- added REF**: KeebTester_logo, AtariKeyboardTester:KeebTester_logo, F.Cu at (32.4, 38.1)
- added REF**: OSH_logo, Atari130MX:OSH_logo, F.Cu at (139.1, 27.9)
- added REF**: MountingHole_2.2mm_M2, MountingHole:MountingHole_2.2mm_M2, F.Cu at (146.7, 24.1)
- added REF**: MountingHole_2.2mm_M2, MountingHole:MountingHole_2.2mm_M2, F.Cu at (146.7, 142.9)
- added REF**: MountingHole_2.2mm_M2, MountingHole:MountingHole_2.2mm_M2, F.Cu at (23.5, 142.9)
- added REF**: MountingHole_2.2mm_M2, MountingHole:MountingHole_2.2mm_M2, F.Cu at (23.5, 24.1)
- added XL/XE configuration: SolderJumper_3_Open, AtariKeyboardTester:PinHeader_1x03_P2.54mm_Vertical, F.Cu at (33.0, 78.7)
- , [: renamed from D_,_1
- . ]: renamed from D_._1
- / ?: renamed from D_/_1
- 2x AAA: renamed from BT1
- Atari Connector: renamed from J1
- FFC 1-25 3-26: renamed from J4
- Pin headers: renamed from J2
- R1, R2, R3: value R -> 100; footprint Resistor_THT:R_Axial_DIN0207_L6.3mm_D2.5mm_P7.62mm_Horizontal -> AtariKeyboardTester:R100
- R10, R11, R12, R13, R14, R15, R16, R17, R18, R19, R20, R21, R22, R23, R24, R4, R5, R6, R7, R8, R9, R_LED_COL_1, R_LED_COL_10, R_LED_COL_11, R_LED_COL_12, R_LED_COL_13, R_LED_COL_14, R_LED_COL_2, R_LED_COL_3, R_LED_COL_4, R_LED_COL_5, R_LED_COL_6, R_LED_COL_7, R_LED_COL_8, R_LED_COL_9: footprint Resistor_THT:R_Axial_DIN0207_L6.3mm_D2.5mm_P7.62mm_Horizontal -> AtariKeyboardTester:R100
- renumbered D_B_1 to B, D_C_1 to C, D_Caps_1 to Caps, J3 to IDC, D_Inv_1 to Inv, D_M_1 to M, D_N_1 to N, D_Shift_2 to Shift, D_Shift_1 to Shift, D_SPACE_1 to Space, D_V_1 to V, D_X_1 to X, D_Z_1 to Z
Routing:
- net ROW_9: track 0.00 -> 294.6 mm
- net ROW_1: track 0.00 -> 280.9 mm, vias 0 -> 3
- net ROW_2: track 0.00 -> 230.2 mm, vias 0 -> 4
- net COL_14: track 34.4 -> 225.3 mm
- net ROW_3: track 0.00 -> 179.6 mm, vias 0 -> 2
- net ROW_6: track 0.00 -> 177.5 mm, vias 0 -> 4
- net ROW_5: track 0.00 -> 176.5 mm, vias 0 -> 6
- net ROW_7: track 0.00 -> 171.6 mm
- net ROW_8: track 0.00 -> 167.1 mm, vias 0 -> 1
- net ROW_4: track 0.00 -> 145.4 mm, vias 0 -> 3
- net COL_9: track 11.1 -> 46.8 mm
- net COL_1: track 29.4 -> 64.5 mm, vias 0 -> 1
- net COL_2: track 11.4 -> 43.0 mm, vias 0 -> 1
- net COL_3: track 9.57 -> 25.0 mm
- net COL_4: track 10.9 -> 24.2 mm
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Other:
- board outline added: 129.5 x 125.1 mm
- board text added: "XE"
- board text added: "XL"
